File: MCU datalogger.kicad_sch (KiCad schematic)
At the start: 25 parts, among them U1 24LC1025, U2 24LC1025, U3 ATMEGA328P-AU, U4 DS1337S_, Y1 32.768 KHz, Y2 16MHz

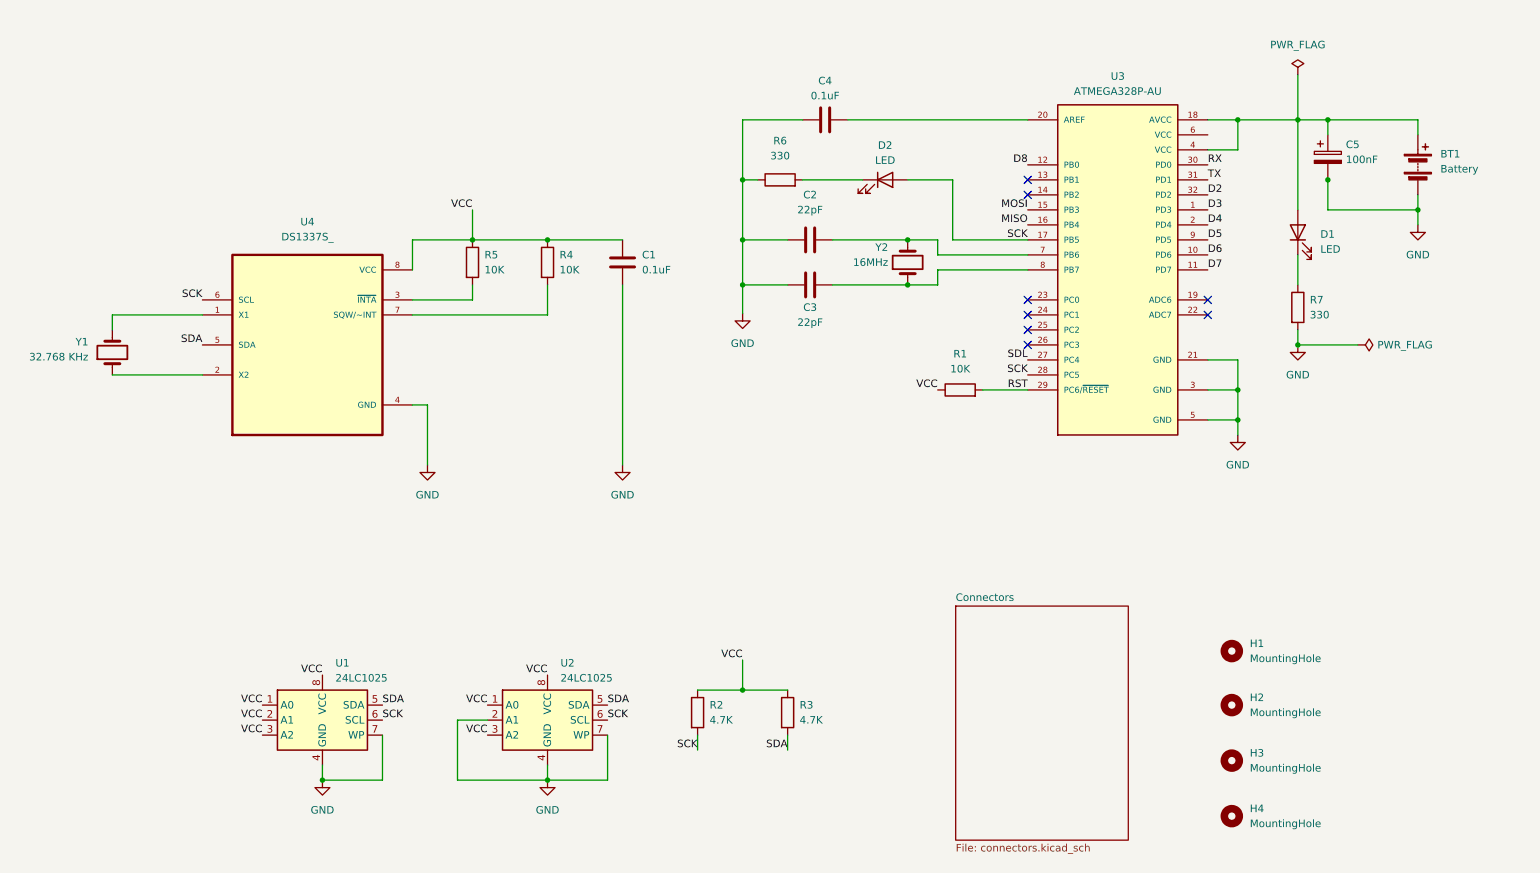
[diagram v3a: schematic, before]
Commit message: Completed the wiring including second sheet
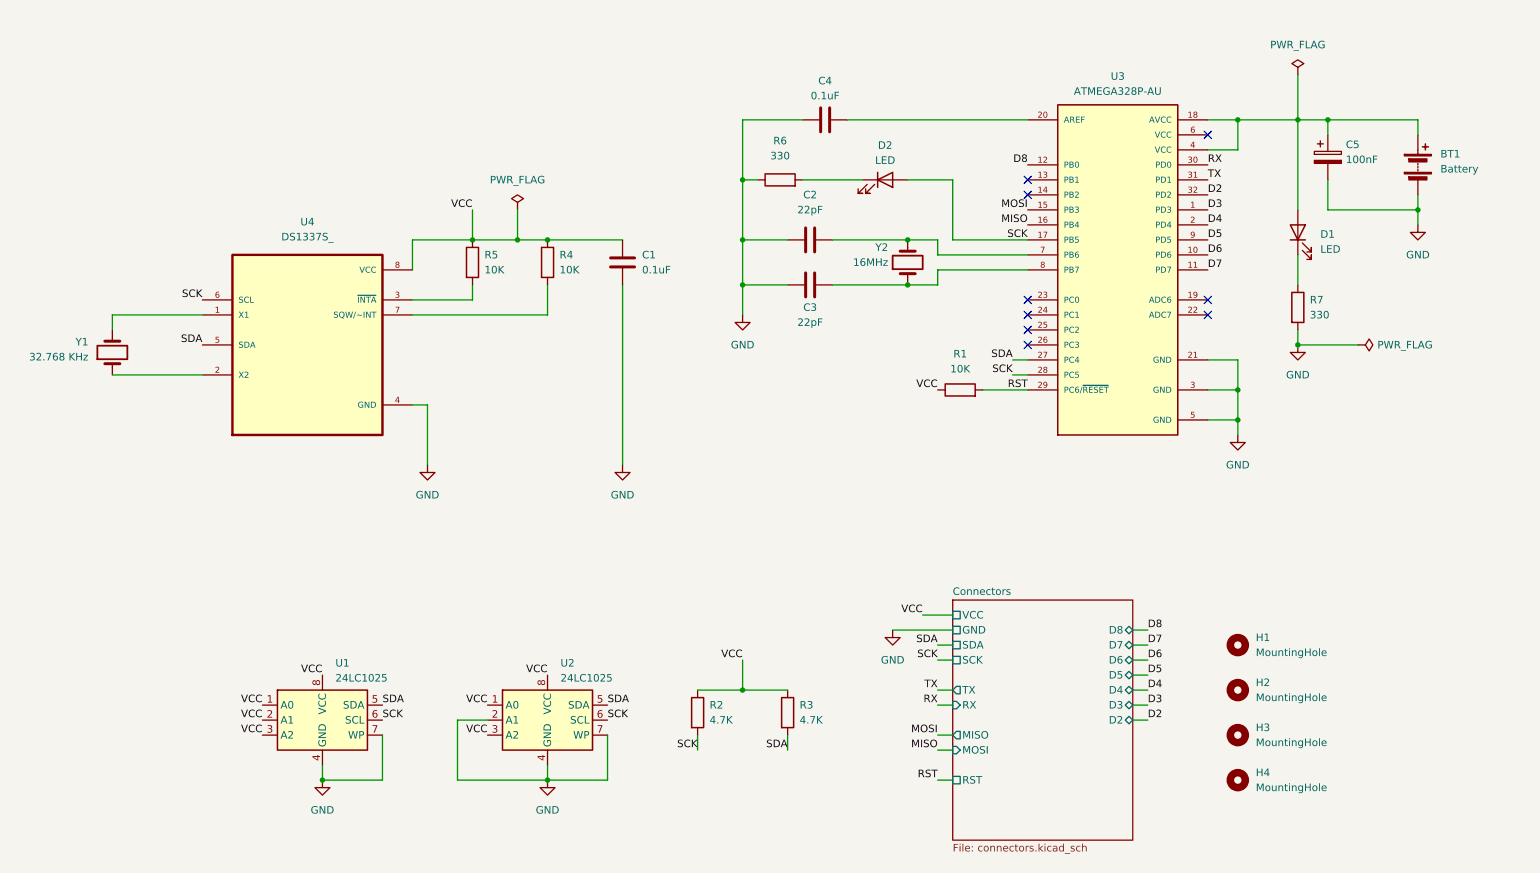
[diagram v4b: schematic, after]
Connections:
- net SDL is gone; now on net SDA: U3.27 (PC4)
- no-connect marks 8 -> 9
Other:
- sheet Connectors ports: added D2, D3, D4, D5, D6, D7, D8, GND, MISO, MOSI, RST, RX, SCK, SDA, TX, VCC; removed none
- moved on the sheet: H1, H2, H3, H4

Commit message: Completed comments
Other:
- note added: "EEPROM"
- note added: "MCU"
- note added: "Mounting"
- note added: "Real time clock"
- moved on the sheet: C1, R4, U4, Y1

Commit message: routing complete
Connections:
- net VCC: now also BT1.1 (+), C5.1, D1.2 (A), U3.18 (AVCC), U3.4 (VCC)
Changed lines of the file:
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@@
+		)
+	)
+	(label "VCC"
+		(at 246.38 35.56 180)
+		(effects
+			(font
+				(size 1.27 1.27)
+			)
+			(justify right bottom)
 		)
 	)

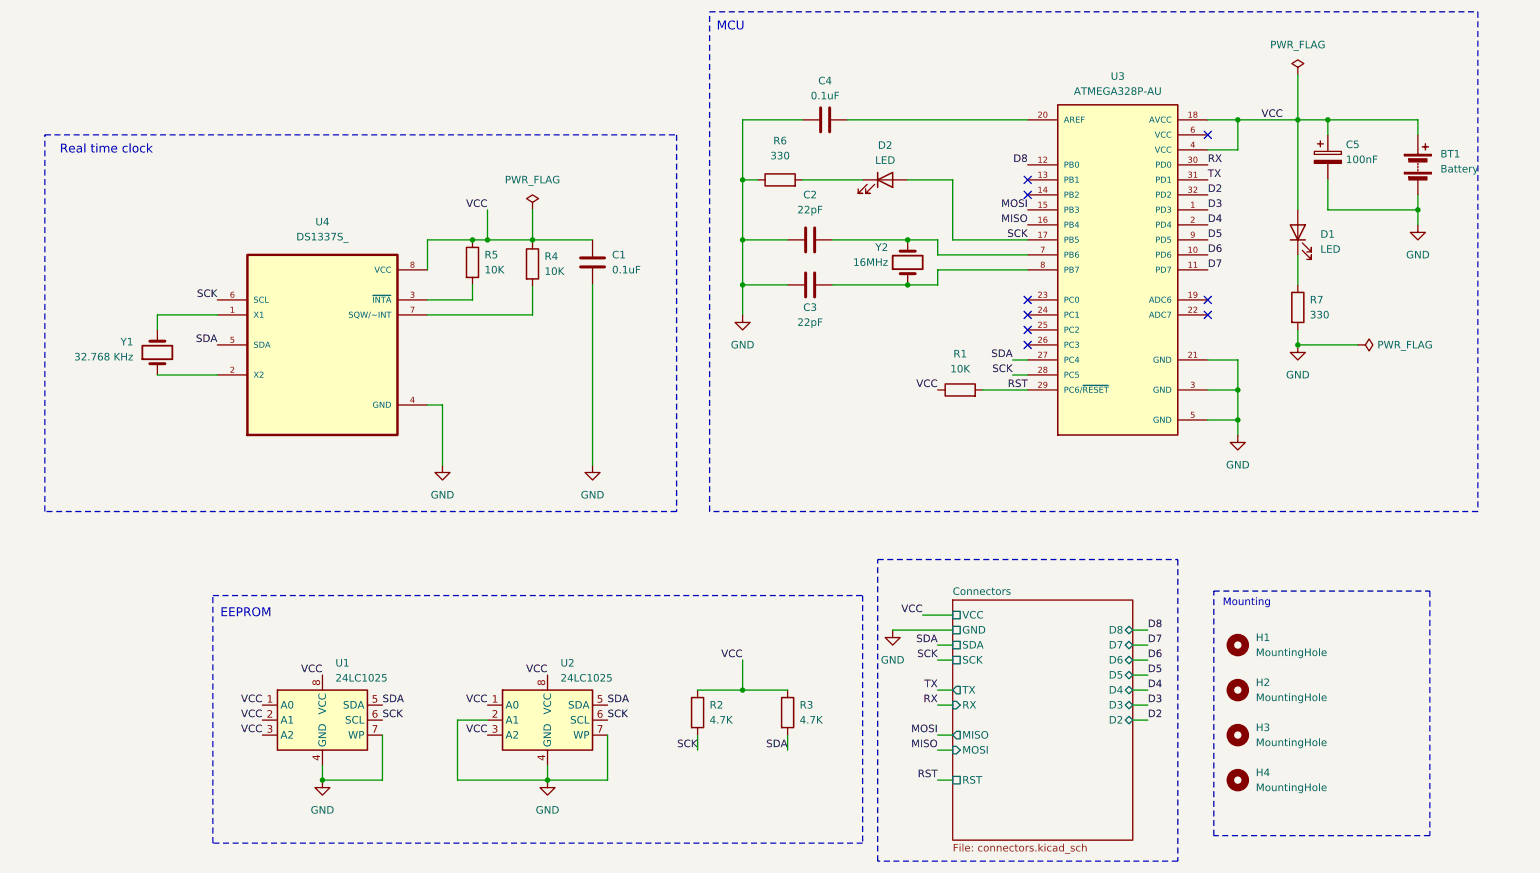
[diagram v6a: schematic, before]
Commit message: Fixed two defects in schematic.
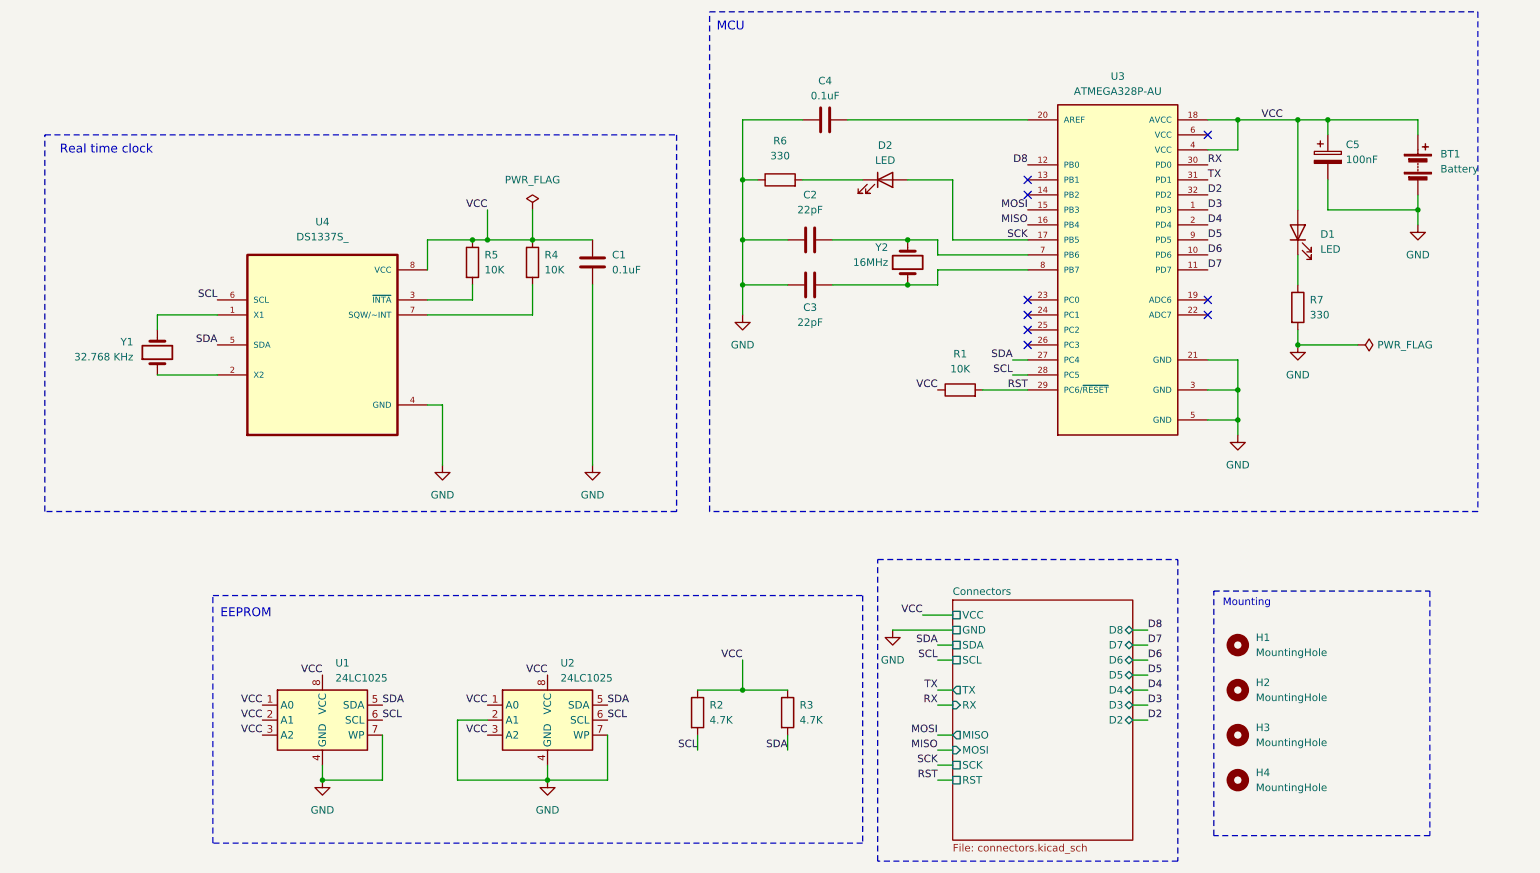
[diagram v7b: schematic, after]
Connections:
- net SCK: no longer R2.2, U1.6 (SCL), U2.6 (SCL), U3.28 (PC5), U4.6 (SCL)
- new net SCL: R2.2, U1.6 (SCL), U2.6 (SCL), U3.28 (PC5), U4.6 (SCL)
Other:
- sheet Connectors ports: added SCL; removed none
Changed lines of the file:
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@@
 	(wire
 		(pts
-			(xy 119.38 63.754) (xy 119.38 68.58)
+			(xy 119.38 63.5) (xy 119.38 68.58)
 		)
 		(stroke
@@
 	(wire
 		(pts
+			(xy 187.96 144.78) (xy 190.5 144.78)
+		)
+		(stroke
+			(width 0)
+			(type default)
+		)
+	)
+	(wire
+		(pts
 			(xy 238.76 88.9) (xy 238.76 86.36)
 		)
@@
 	(wire
 		(pts
-			(xy 248.92 27.94) (xy 248.92 35.56)
-		)
-		(stroke
-			(width 0)
-			(type default)
-		)
-	)
-	(wire
-		(pts
 			(xy 187.96 55.88) (xy 187.96 58.42)
 		)
@@
 	(wire
 		(pts
-			(xy 119.38 56.134) (xy 119.38 55.88)
-		)
-		(stroke
-			(width 0)
-			(type default)
-		)
-	)
-	(wire
-		(pts
 			(xy 172.72 35.56) (xy 203.2 35.56)
 		)
@@
 		)
 	)
-	(label "SCK"
+	(label "SCL"
 		(at 147.32 142.24 180)
 		(effects
@@
 		)
 	)
-	(label "SCK"
+	(label "SCL"
 		(at 132.08 137.16 0)
 		(effects
@@
 		)
 	)
-	(label "SCK"
+	(label "SCL"
 		(at 187.96 127 180)
 		(effects
@@
 		)
 	)
+	(label "SCK"
+		(at 187.96 144.78 180)
+		(effects
+			(font
+				(size 1.27 1.27)
+			)
+			(justify right bottom)
+		)
+	)
 	(label "D3"
 		(at 233.68 50.8 0)
@@
 		)
 	)
-	(label "SCK"
+	(label "SCL"
 		(at 66.04 66.04 180)
 		(effects
@@
 		)
 	)
-	(label "SCK"
+	(label "SCL"
 		(at 200.66 78.74 180)
 		(effects
@@
 		)
 	)
-	(label "SCK"
+	(label "SCL"
 		(at 93.98 137.16 0)
 		(effects
@@
 	(symbol
 		(lib_id "Device:R")
-		(at 119.38 59.944 0)
+		(at 119.38 59.69 0)
 		(unit 1)
 		(exclude_from_sim no)
@@
 		(fields_autoplaced yes)
 		(property "Reference" "R4"
-			(at 121.412 58.6739 0)
+			(at 121.412 58.4199 0)
 			(effects
 				(font
@@
 		)
 		(property "Value" "10K"
-			(at 121.412 61.2139 0)
+			(at 121.412 60.9599 0)
 			(effects
 				(font
@@
 		)
 		(property "Footprint" "Resistor_SMD:R_0805_2012Metric"
-			(at 117.602 59.944 90)
+			(at 117.602 59.69 90)
 			(effects
 				(font
@@
 		)
 		(property "Datasheet" "~"
-			(at 119.38 59.944 0)
+			(at 119.38 59.69 0)
 			(effects
 				(font
@@
 		)
 		(property "Description" "Resistor"
-			(at 119.38 59.944 0)
+			(at 119.38 59.69 0)
 			(effects
 				(font
@@
 		)
 		(property "Purpose" ""
-			(at 119.38 59.944 0)
+			(at 119.38 59.69 0)
 			(effects
 				(font
@@
 	)
 	(symbol
-		(lib_id "power:PWR_FLAG")
-		(at 248.92 27.94 0)
-		(unit 1)
-		(exclude_from_sim no)
-		(in_bom yes)
-		(on_board yes)
-		(dnp no)
-		(fields_autoplaced yes)
-		(property "Reference" "#FLG01"
-			(at 248.92 26.035 0)
-			(effects
-				(font
-					(size 1.27 1.27)
-				)
-				(hide yes)
-			)
-		)
-		(property "Value" "PWR_FLAG"
-			(at 248.92 22.86 0)
-			(effects
-				(font
-					(size 1.27 1.27)
-				)
-			)
-		)
-		(property "Footprint" ""
-			(at 248.92 27.94 0)
-			(effects
-				(font
-					(size 1.27 1.27)
-				)
-				(hide yes)
-			)
-		)
-		(property "Datasheet" "~"
-			(at 248.92 27.94 0)
-			(effects
-				(font
-					(size 1.27 1.27)
-				)
-				(hide yes)
-			)
-		)
-		(property "Description" "Special symbol for telling ERC where power comes from"
-			(at 248.92 27.94 0)
-			(effects
-				(font
-					(size 1.27 1.27)
-				)
-				(hide yes)
-			)
-		)
-		(pin "1"
-		)
-		(instances
-			(project ""
-				(path "/9000079e-69eb-4cef-8509-5557f3341200"
-					(reference "#FLG01")
-					(unit 1)
-				)
-			)
-		)
-	)
-	(symbol
 		(lib_name "24LC1025_1")
 		(lib_id "Memory_EEPROM:24LC1025")
@@
 			)
 		)
-		(pin "SCK" passive
+		(pin "SCL" passive
 			(at 190.5 127 180)
 			(effects
@@
 			(effects
 				(font
+					(size 1.27 1.27)
+				)
+				(justify left)
+			)
+		)
+		(pin "SCK" passive
+			(at 190.5 144.78 180)
+			(effects
+				(font
